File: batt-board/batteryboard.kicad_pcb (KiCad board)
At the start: 2 copper layers, 95.9 x 90.2 mm, 30 parts, among them J1 KEYSTONE-1042, J10 Screw_Terminal_01x02, J11 Screw_Terminal_01x02, J12 Screw_Terminal_01x01, J2 KEYSTONE-1042, J3 KEYSTONE-1042, J4 KEYSTONE-1042, J7 JST_PH_S2B-PH-SM4, J8 Screw_Terminal_01x02, J9 Screw_Terminal_01x02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

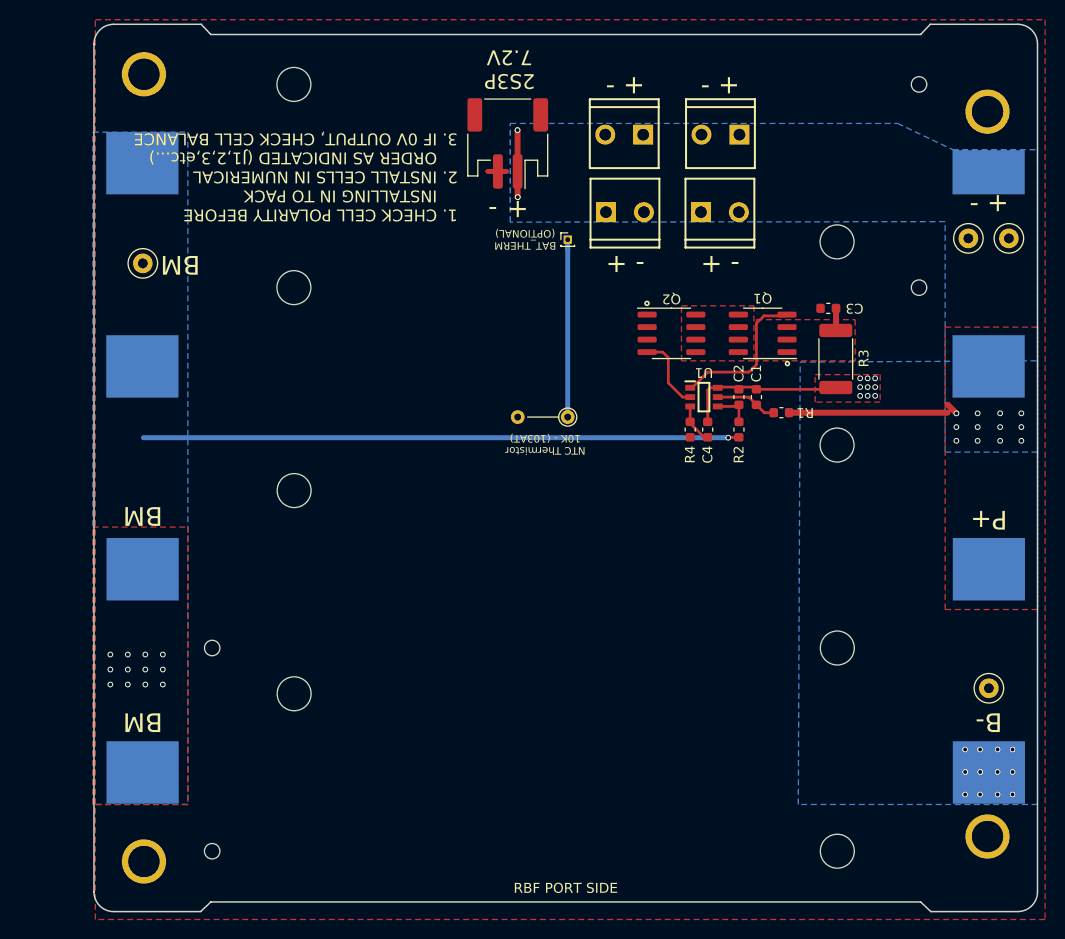
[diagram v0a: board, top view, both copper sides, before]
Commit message: modified batt board to have wiring cutouts
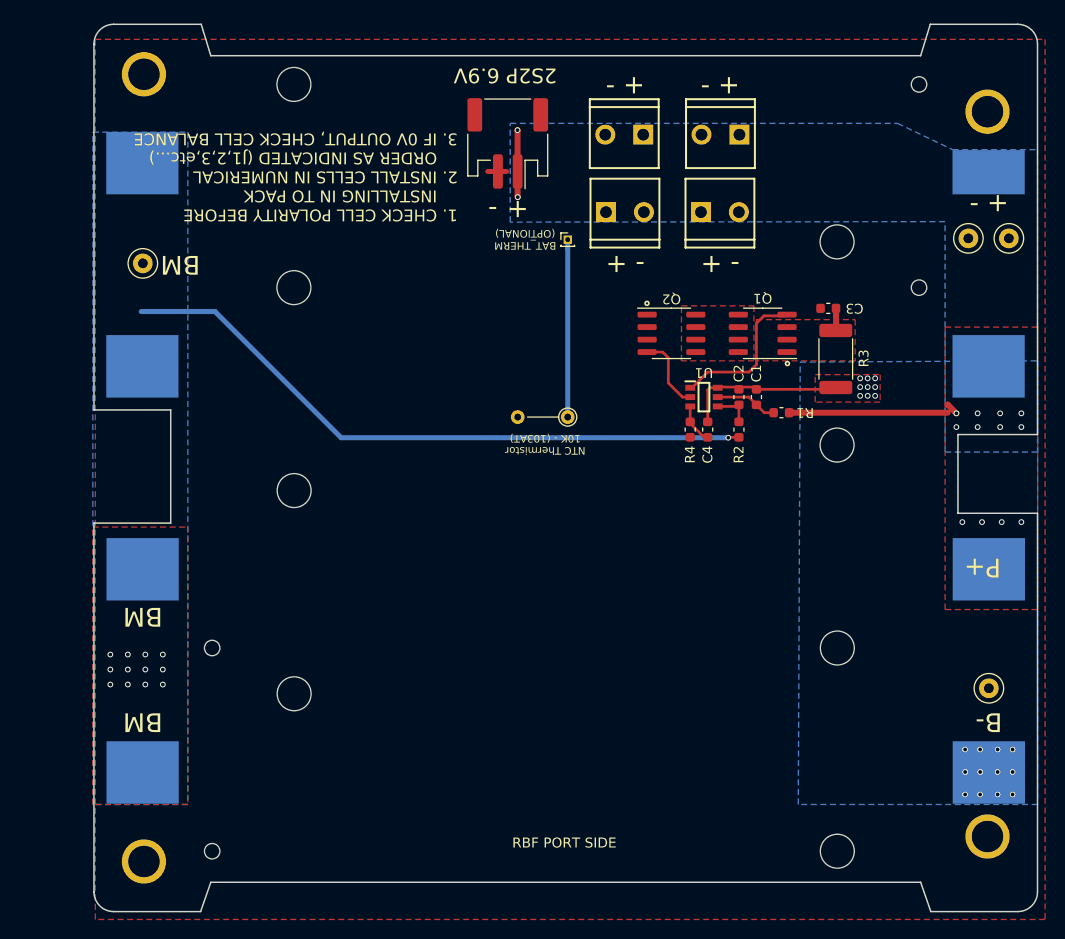
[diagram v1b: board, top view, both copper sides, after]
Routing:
- net BM: track 60.5 -> 66.1 mm
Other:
- outline, holes or cut-outs redrawn
- board text added: "2S2P 6.9V"
- board text removed: "2S3P 7.2V"
- board text removed: "HOLLIDAY"
